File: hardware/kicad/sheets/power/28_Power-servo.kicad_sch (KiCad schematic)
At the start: 18 parts, among them U22 TPSM63610RDFR

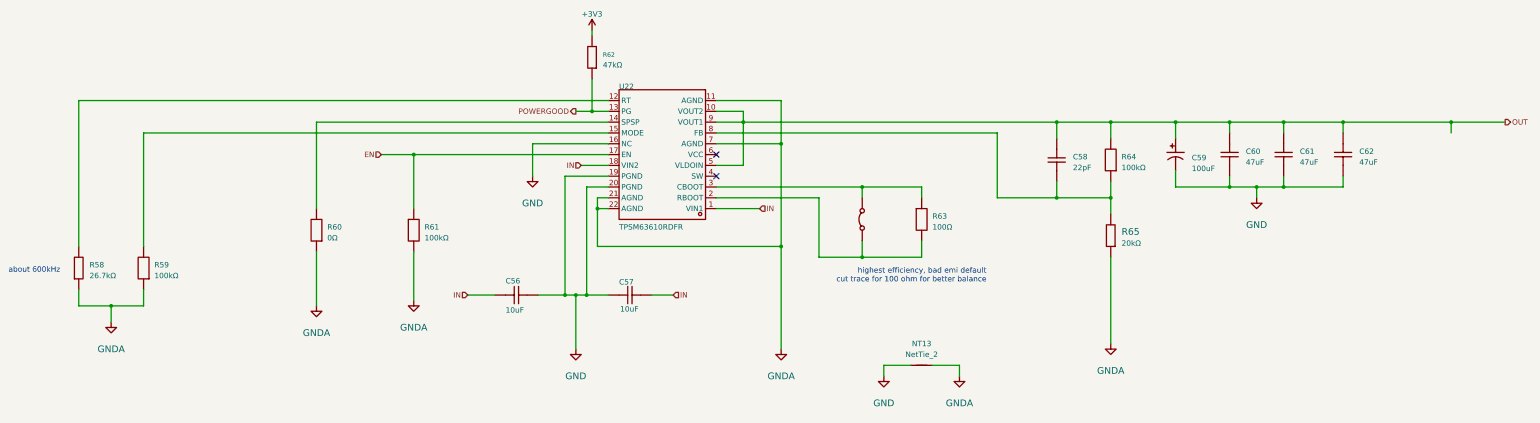
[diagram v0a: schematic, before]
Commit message: current sensing on the servos and cleaning up empty sheets
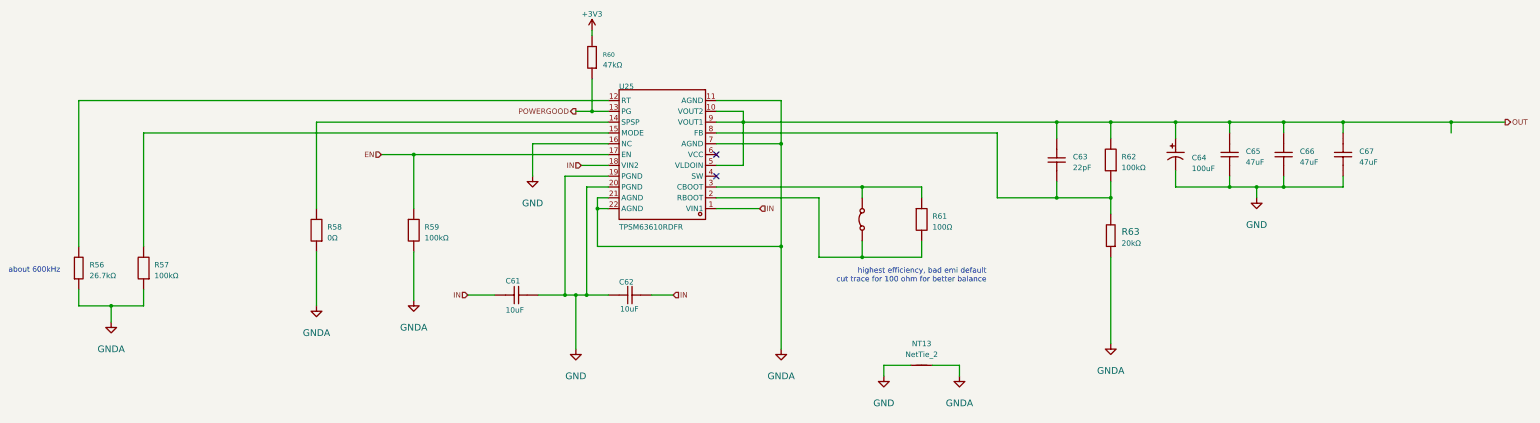
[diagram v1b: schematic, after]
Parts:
- renumbered C56 to C61, C57 to C62, C58 to C63, C59 to C64, C60 to C65, C61 to C66, C62 to C67, R58 to R56, R59 to R57, R60 to R58, R61 to R59, R62 to R60, R63 to R61, R64 to R62, R65 to R63, U22 to U25, U23 to U26

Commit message: starting pcb
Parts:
- NT13: footprint (none) -> NetTie:NetTie-2_SMD_Pad2.0mm
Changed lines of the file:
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@@
 			)
 		)
-		(property "Footprint" ""
+		(property "Footprint" "NetTie:NetTie-2_SMD_Pad2.0mm"
 			(at 234.95 142.24 0)
 			(effects

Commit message: new references
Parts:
- renumbered C61 to C63, C62 to C64, C63 to C65, C64 to C66, C65 to C67, C66 to C68, C67 to C69, R56 to R79, R57 to R80, R58 to R81, R59 to R82, R60 to R83, R61 to R84, R62 to R85, R63 to R86, U25 to U31, U26 to U32

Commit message: pre robot updating references
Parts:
- renumbered C63 to C62, C64 to C63, C65 to C64, C66 to C65, C67 to C66, C68 to C67, C69 to C68, NT13 to NT16, R79 to R87, R80 to R88, R81 to R89, R82 to R90, R83 to R91, R84 to R92, R85 to R93, R86 to R94, U31 to U32, U32 to U33

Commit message: various imprvements
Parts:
- renumbered C62 to C67, C63 to C68, C64 to C69, C65 to C70, C66 to C71, C67 to C72, C68 to C73, R87 to R117, R88 to R118, R89 to R119, R90 to R120, R91 to R121, R92 to R122, R93 to R123, R94 to R124, U32 to U38, U33 to U39
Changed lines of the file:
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@@
 		(on_board yes)
 		(dnp no)
-		(property "Reference" "C66"
+		(property "Reference" "C71"
 			(at 311.15 92.71 90)
 			(effects
@@
 			(project "svea_powerboard_rev3"
 				(path "/3f85abf4-0b95-4c4a-b7e9-06f59ca1ea3d/5c2e021f-c2d4-49e2-8c36-9a64f1f12001/5e87fa27-0735-4860-928c-5f9d8795dad6"
-					(reference "C66")
+					(reference "C71")
 					(unit 1)
 				)
@@
 		(on_board yes)
 		(dnp no)
-		(property "Reference" "C64"
+		(property "Reference" "C69"
 			(at 270.51 93.98 90)
 			(effects
@@
 			(project "svea_powerboard_rev3"
 				(path "/3f85abf4-0b95-4c4a-b7e9-06f59ca1ea3d/5c2e021f-c2d4-49e2-8c36-9a64f1f12001/5e87fa27-0735-4860-928c-5f9d8795dad6"
-					(reference "C64")
+					(reference "C69")
 					(unit 1)
 				)
@@
 		(on_board yes)
 		(dnp no)
-		(property "Reference" "C65"
+		(property "Reference" "C70"
 			(at 298.45 92.71 90)
 			(effects
@@
 			(project "svea_powerboard_rev3"
 				(path "/3f85abf4-0b95-4c4a-b7e9-06f59ca1ea3d/5c2e021f-c2d4-49e2-8c36-9a64f1f12001/5e87fa27-0735-4860-928c-5f9d8795dad6"
-					(reference "C65")
+					(reference "C70")
 					(unit 1)
 				)
@@
 		(on_board yes)
 		(dnp no)
-		(property "Reference" "R94"
+		(property "Reference" "R124"
 			(at 281.94 111.76 90)
 			(effects
@@
 			(project "svea_powerboard_rev3"
 				(path "/3f85abf4-0b95-4c4a-b7e9-06f59ca1ea3d/5c2e021f-c2d4-49e2-8c36-9a64f1f12001/5e87fa27-0735-4860-928c-5f9d8795dad6"
-					(reference "R94")
+					(reference "R124")
 					(unit 1)
 				)
@@
 		(on_board yes)
 		(dnp no)
-		(property "Reference" "C62"
+		(property "Reference" "C67"
 			(at 137.16 121.666 90)
 			(effects
@@
 			(project "svea_powerboard_rev3"
 				(path "/3f85abf4-0b95-4c4a-b7e9-06f59ca1ea3d/5c2e021f-c2d4-49e2-8c36-9a64f1f12001/5e87fa27-0735-4860-928c-5f9d8795dad6"
-					(reference "C62")
+					(reference "C67")
 					(unit 1)
 				)
@@
 		(on_board yes)
 		(dnp no)
-		(property "Reference" "C68"
+		(property "Reference" "C73"
 			(at 337.82 92.71 90)
 			(effects
@@
 			(project "svea_powerboard_rev3"
 				(path "/3f85abf4-0b95-4c4a-b7e9-06f59ca1ea3d/5c2e021f-c2d4-49e2-8c36-9a64f1f12001/5e87fa27-0735-4860-928c-5f9d8795dad6"
-					(reference "C68")
+					(reference "C73")
 					(unit 1)
 				)
@@
 		(on_board yes)
 		(dnp no)
-		(property "Reference" "U33"
+		(property "Reference" "U39"
 			(at 220.98 107.95 90)
 			(effects
@@
 			(project "svea_powerboard_rev3"
 				(path "/3f85abf4-0b95-4c4a-b7e9-06f59ca1ea3d/5c2e021f-c2d4-49e2-8c36-9a64f1f12001/5e87fa27-0735-4860-928c-5f9d8795dad6"
-					(reference "U33")
+					(reference "U39")
 					(unit 1)
 				)
@@
 		(on_board yes)
 		(dnp no)
-		(property "Reference" "#PWR0103"
+		(property "Reference" "#PWR0116"
 			(at 243.84 144.78 0)
 			(effects
@@
 			(project "svea_powerboard_rev3"
 				(path "/3f85abf4-0b95-4c4a-b7e9-06f59ca1ea3d/5c2e021f-c2d4-49e2-8c36-9a64f1f12001/5e87fa27-0735-4860-928c-5f9d8795dad6"
-					(reference "#PWR0103")
+					(reference "#PWR0116")
 					(unit 1)
 				)
@@
 		(on_board yes)
 		(dnp no)
-		(property "Reference" "R89"
+		(property "Reference" "R119"
 			(at 95.25 110.49 90)
 			(effects
@@
 			(project "svea_powerboard_rev3"
 				(path "/3f85abf4-0b95-4c4a-b7e9-06f59ca1ea3d/5c2e021f-c2d4-49e2-8c36-9a64f1f12001/5e87fa27-0735-4860-928c-5f9d8795dad6"
-					(reference "R89")
+					(reference "R119")
 					(unit 1)
 				)
@@
 		(on_board yes)
 		(dnp no)
-		(property "Reference" "C63"
+		(property "Reference" "C68"
 			(at 163.83 121.92 90)
 			(effects
@@
 			(project "svea_powerboard_rev3"
 				(path "/3f85abf4-0b95-4c4a-b7e9-06f59ca1ea3d/5c2e021f-c2d4-49e2-8c36-9a64f1f12001/5e87fa27-0735-4860-928c-5f9d8795dad6"
-					(reference "C63")
+					(reference "C68")
 					(unit 1)
 				)
@@
 		(on_board yes)
 		(dnp no)
-		(property "Reference" "R93"
+		(property "Reference" "R123"
 			(at 281.94 93.98 90)
 			(effects
@@
 			(project "svea_powerboard_rev3"
 				(path "/3f85abf4-0b95-4c4a-b7e9-06f59ca1ea3d/5c2e021f-c2d4-49e2-8c36-9a64f1f12001/5e87fa27-0735-4860-928c-5f9d8795dad6"
-					(reference "R93")
+					(reference "R123")
 					(unit 1)
 				)
@@
 		(on_board yes)
 		(dnp no)
-		(property "Reference" "#PWR097"
+		(property "Reference" "#PWR0110"
 			(at 44.45 132.08 0)
 			(effects
@@
 			(project "svea_powerboard_rev3"
 				(path "/3f85abf4-0b95-4c4a-b7e9-06f59ca1ea3d/5c2e021f-c2d4-49e2-8c36-9a64f1f12001/5e87fa27-0735-4860-928c-5f9d8795dad6"
-					(reference "#PWR097")
+					(reference "#PWR0110")
 					(unit 1)
 				)
@@
 		(on_board yes)
 		(dnp no)
-		(property "Reference" "#PWR0104"
+		(property "Reference" "#PWR0117"
 			(at 279.4 137.16 0)
 			(effects
@@
 			(project "svea_powerboard_rev3"
 				(path "/3f85abf4-0b95-4c4a-b7e9-06f59ca1ea3d/5c2e021f-c2d4-49e2-8c36-9a64f1f12001/5e87fa27-0735-4860-928c-5f9d8795dad6"
-					(reference "#PWR0104")
+					(reference "#PWR0117")
 					(unit 1)
 				)
@@
 		(on_board yes)
 		(dnp no)
-		(property "Reference" "R87"
+		(property "Reference" "R117"
 			(at 39.37 119.38 90)
 			(effects
@@
 			(project "svea_powerboard_rev3"
 				(path "/3f85abf4-0b95-4c4a-b7e9-06f59ca1ea3d/5c2e021f-c2d4-49e2-8c36-9a64f1f12001/5e87fa27-0735-4860-928c-5f9d8795dad6"
-					(reference "R87")
+					(reference "R117")
 					(unit 1)
 				)
@@
 		(on_board yes)
 		(dnp no)
-		(property "Reference" "R91"
+		(property "Reference" "R121"
 			(at 160.02 69.85 90)
 			(effects
@@
 			(project "svea_powerboard_rev3"
 				(path "/3f85abf4-0b95-4c4a-b7e9-06f59ca1ea3d/5c2e021f-c2d4-49e2-8c36-9a64f1f12001/5e87fa27-0735-4860-928c-5f9d8795dad6"
-					(reference "R91")
+					(reference "R121")
 					(unit 1)
 				)
@@
 		(on_board yes)
 		(dnp no)
-		(property "Reference" "#PWR099"
+		(property "Reference" "#PWR0112"
 			(at 115.57 127 0)
 			(effects
@@
 			(project "svea_powerboard_rev3"
 				(path "/3f85abf4-0b95-4c4a-b7e9-06f59ca1ea3d/5c2e021f-c2d4-49e2-8c36-9a64f1f12001/5e87fa27-0735-4860-928c-5f9d8795dad6"
-					(reference "#PWR099")
+					(reference "#PWR0112")
 					(unit 1)
 				)
@@
 		(on_board yes)
 		(dnp no)
-		(property "Reference" "R92"
+		(property "Reference" "R122"
 			(at 237.49 107.95 90)
 			(effects
@@
 			(project "svea_powerboard_rev3"
 				(path "/3f85abf4-0b95-4c4a-b7e9-06f59ca1ea3d/5c2e021f-c2d4-49e2-8c36-9a64f1f12001/5e87fa27-0735-4860-928c-5f9d8795dad6"
-					(reference "R92")
+					(reference "R122")
 					(unit 1)
 				)
@@
 		(on_board yes)
 		(dnp no)
-		(property "Reference" "C67"
+		(property "Reference" "C72"
 			(at 323.85 92.71 90)
 			(effects
@@
 			(project "svea_powerboard_rev3"
 				(path "/3f85abf4-0b95-4c4a-b7e9-06f59ca1ea3d/5c2e021f-c2d4-49e2-8c36-9a64f1f12001/5e87fa27-0735-4860-928c-5f9d8795dad6"
-					(reference "C67")
+					(reference "C72")
 					(unit 1)
 				)
@@
 		(on_board yes)
 		(dnp no)
-		(property "Reference" "#PWR0102"
+		(property "Reference" "#PWR0115"
 			(at 201.93 138.43 0)
 			(effects
@@
 			(project "svea_powerboard_rev3"
 				(path "/3f85abf4-0b95-4c4a-b7e9-06f59ca1ea3d/5c2e021f-c2d4-49e2-8c36-9a64f1f12001/5e87fa27-0735-4860-928c-5f9d8795dad6"
-					(reference "#PWR0102")
+					(reference "#PWR0115")
 					(unit 1)
 				)
@@
 		(on_board yes)
 		(dnp no)
-		(property "Reference" "R90"
+		(property "Reference" "R120"
 			(at 118.11 110.49 90)
 			(effects
@@
 			(project "svea_powerboard_rev3"
 				(path "/3f85abf4-0b95-4c4a-b7e9-06f59ca1ea3d/5c2e021f-c2d4-49e2-8c36-9a64f1f12001/5e87fa27-0735-4860-928c-5f9d8795dad6"
-					(reference "R90")
+					(reference "R120")
 					(unit 1)
 				)
@@
 		(on_board yes)
 		(dnp no)
-		(property "Reference" "#PWR0101"
+		(property "Reference" "#PWR0114"
 			(at 157.48 63.5 0)
 			(effects
@@
 			(project "svea_powerboard_rev3"
 				(path "/3f85abf4-0b95-4c4a-b7e9-06f59ca1ea3d/5c2e021f-c2d4-49e2-8c36-9a64f1f12001/5e87fa27-0735-4860-928c-5f9d8795dad6"
-					(reference "#PWR0101")
+					(reference "#PWR0114")
 					(unit 1)
 				)
@@
 		(on_board yes)
 		(dnp no)
-		(property "Reference" "#PWR098"
+		(property "Reference" "#PWR0111"
 			(at 92.71 128.27 0)
 			(effects
@@
 			(project "svea_powerboard_rev3"
 				(path "/3f85abf4-0b95-4c4a-b7e9-06f59ca1ea3d/5c2e021f-c2d4-49e2-8c36-9a64f1f12001/5e87fa27-0735-4860-928c-5f9d8795dad6"
-					(reference "#PWR098")
+					(reference "#PWR0111")
 					(unit 1)
 				)
@@
 		(on_board yes)
 		(dnp no)
-		(property "Reference" "U32"
+		(property "Reference" "U38"
 			(at 163.83 77.47 0)
 			(effects
@@
 			(project "svea_powerboard_rev3"
 				(path "/3f85abf4-0b95-4c4a-b7e9-06f59ca1ea3d/5c2e021f-c2d4-49e2-8c36-9a64f1f12001/5e87fa27-0735-4860-928c-5f9d8795dad6"
-					(reference "U32")
+					(reference "U38")
 					(unit 1)
 				)
@@
 		(on_board yes)
 		(dnp no)
-		(property "Reference" "R88"
+		(property "Reference" "R118"
 			(at 54.61 119.38 90)
 			(effects
@@
 			(project "svea_powerboard_rev3"
 				(path "/3f85abf4-0b95-4c4a-b7e9-06f59ca1ea3d/5c2e021f-c2d4-49e2-8c36-9a64f1f12001/5e87fa27-0735-4860-928c-5f9d8795dad6"
-					(reference "R88")
+					(reference "R118")
 					(unit 1)
 				)
@@
 		(on_board yes)
 		(dnp no)
-		(property "Reference" "#PWR0100"
+		(property "Reference" "#PWR0113"
 			(at 143.51 97.79 0)
 			(effects
@@
 			(project "svea_powerboard_rev3"
 				(path "/3f85abf4-0b95-4c4a-b7e9-06f59ca1ea3d/5c2e021f-c2d4-49e2-8c36-9a64f1f12001/5e87fa27-0735-4860-928c-5f9d8795dad6"
-					(reference "#PWR0100")
-					(unit 1)
-				)
+					(reference "#PWR0113")
+					(unit 1)
+				)

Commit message: updated some footprints, fixed board
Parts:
- removed R119: 0Ω, Resistor_SMD:R_0603_1608Metric, symbol 5v rail sm-easyedapro:FRC0603F0000TS
- added JP4: Jumper_2_Bridged, Jumper:SolderJumper-2_P1.3mm_Bridged_RoundedPad1.0x1.5mm, symbol Jumper:Jumper_2_Bridged
- renumbered C67 to C65, C68 to C66, C69 to C67, C70 to C68, C71 to C69, C72 to C70, C73 to C71, R117 to R118, R118 to R119, R120 to R121, R121 to R122, R122 to R123, R123 to R124, R124 to R125, U38 to U37, U39 to U38
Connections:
- net GNDA: now also JP4.1 (A)
- net at U37.14 (SPSP): now also JP4.2 (B)
